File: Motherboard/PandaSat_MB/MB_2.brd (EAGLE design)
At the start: 93.9 x 89.2 mm, 165 parts, among them J1 503182-1852, J14 M023.5MM_LOCK, J15 M023.5MM_LOCK, J16 M023.5MM_LOCK, J17 10118194-0001LF, J2 10118194-0001LF, J3 USBC, J4 BU-SMA-V, J5 BK-18650, K4 PE014006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

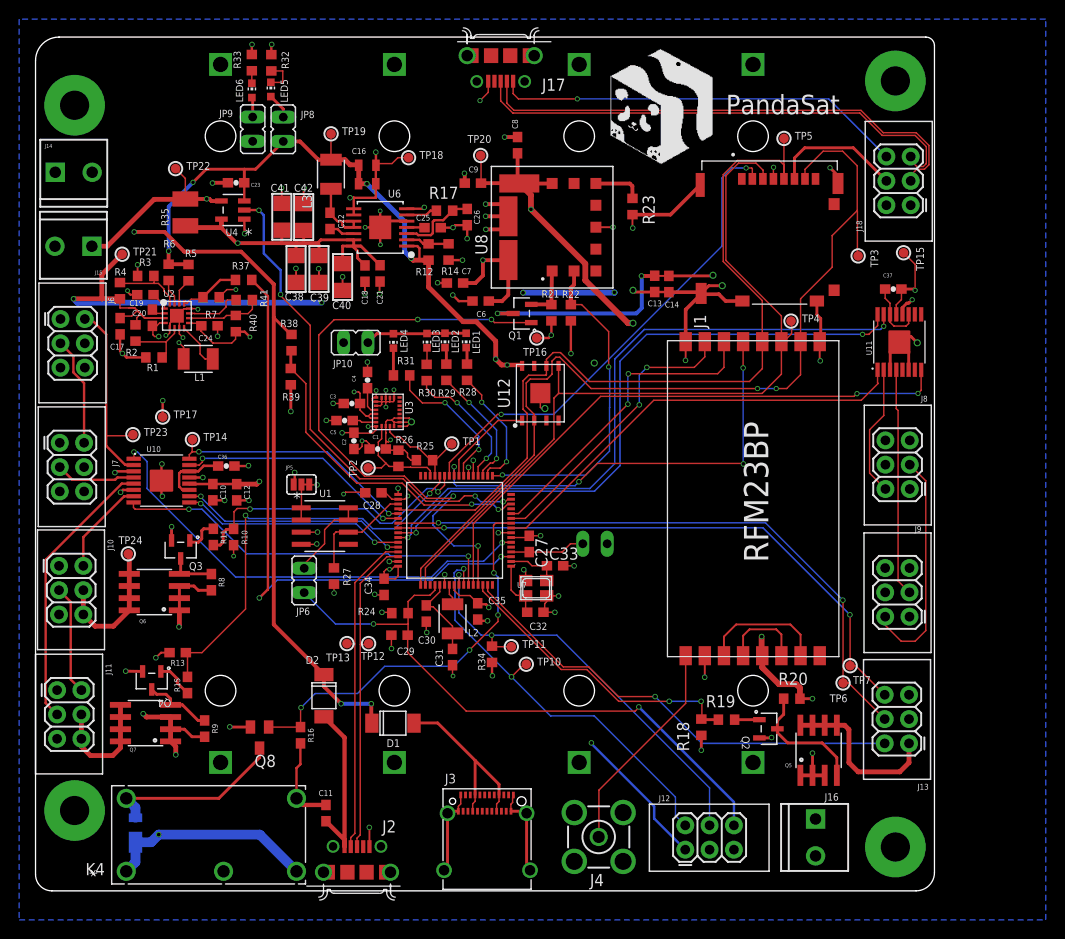
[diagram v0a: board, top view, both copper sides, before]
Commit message: Solar Panel Gerbers Final X, DRC updates for MB
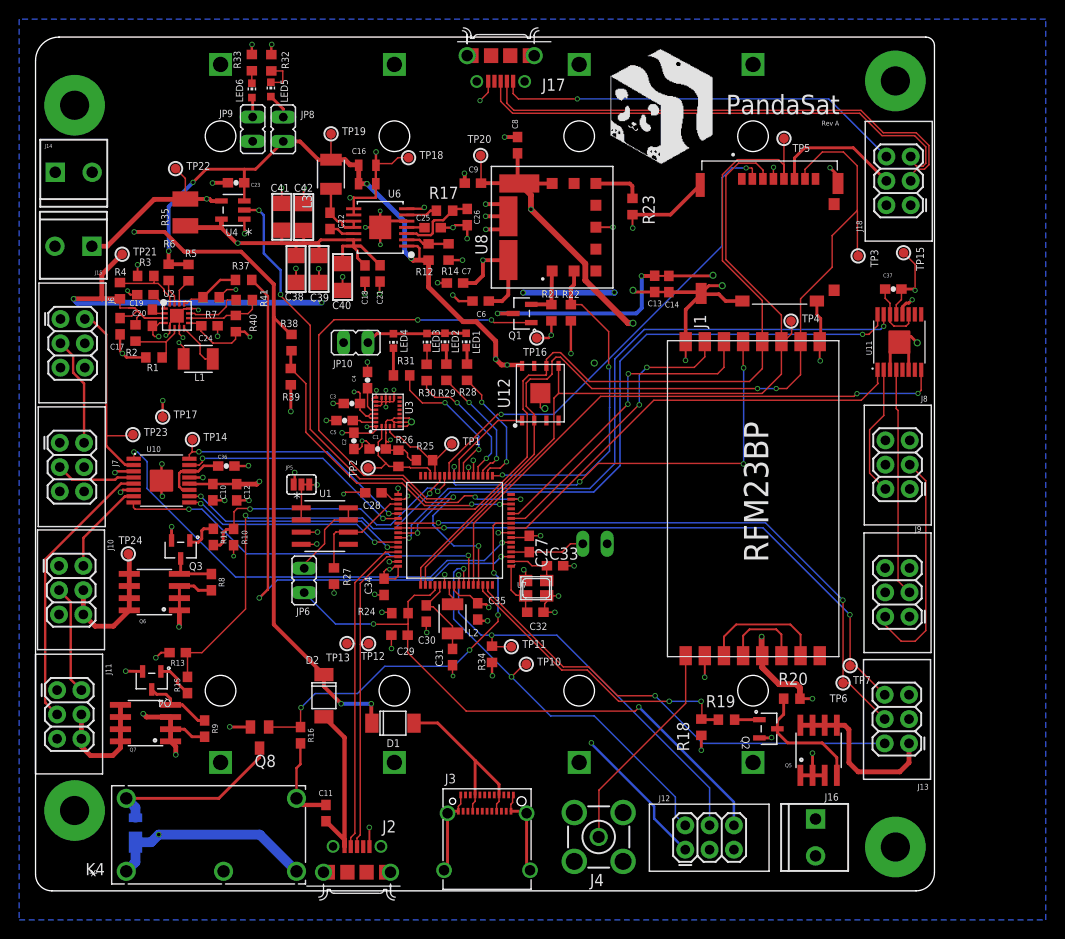
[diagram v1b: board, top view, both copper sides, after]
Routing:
- net I_BATT: track 51.3 -> 53.2 mm
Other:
- board text added: "Rev A"

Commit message: Updated DRC Rules and fixed up errors
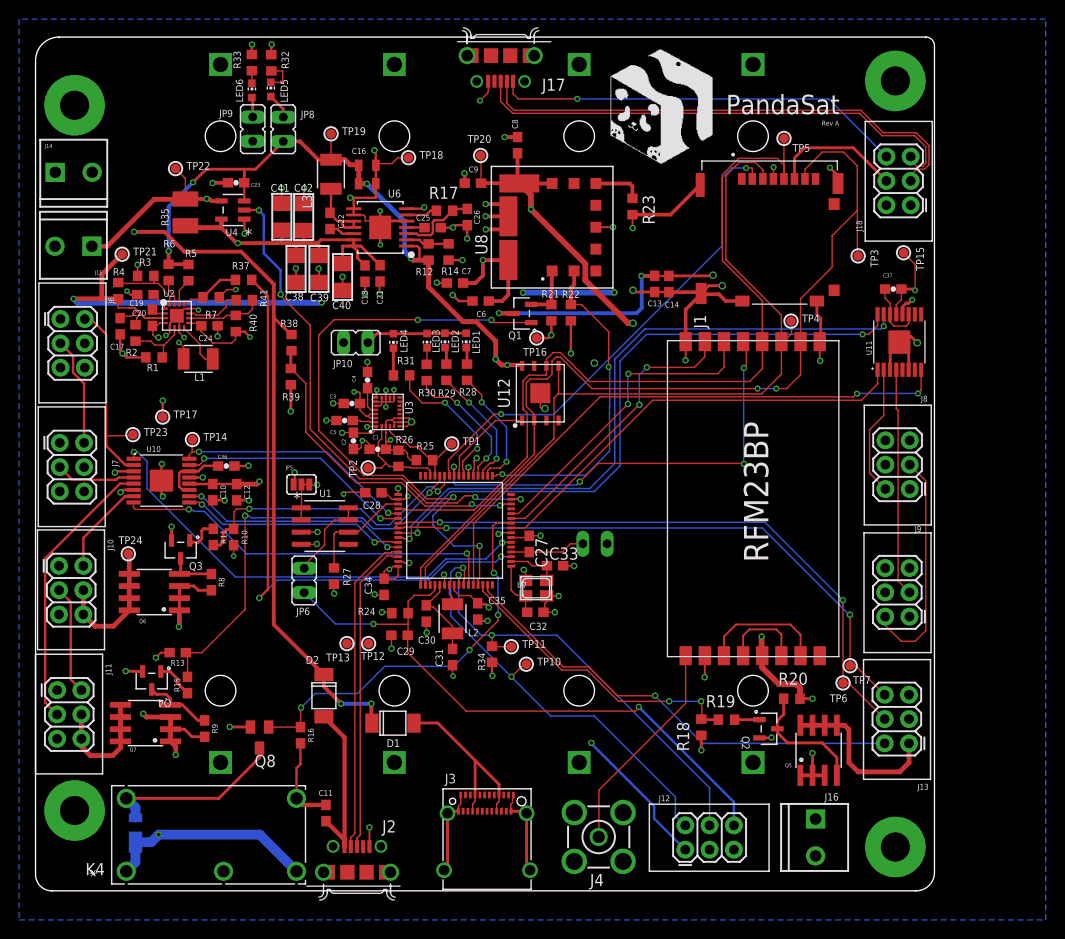
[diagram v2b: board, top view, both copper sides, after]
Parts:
- moved R4 0.18 mm to (-86.2, 63.2)
- moved C2 0.05 mm to (-61.7, 47.5)
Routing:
- net GND: track 260.4 -> 263.6 mm, vias 96 -> 95
- net SWDIO: track 44.1 -> 44.7 mm

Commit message: DRC error fixes, changed footprint for USB-C w/ milling layer
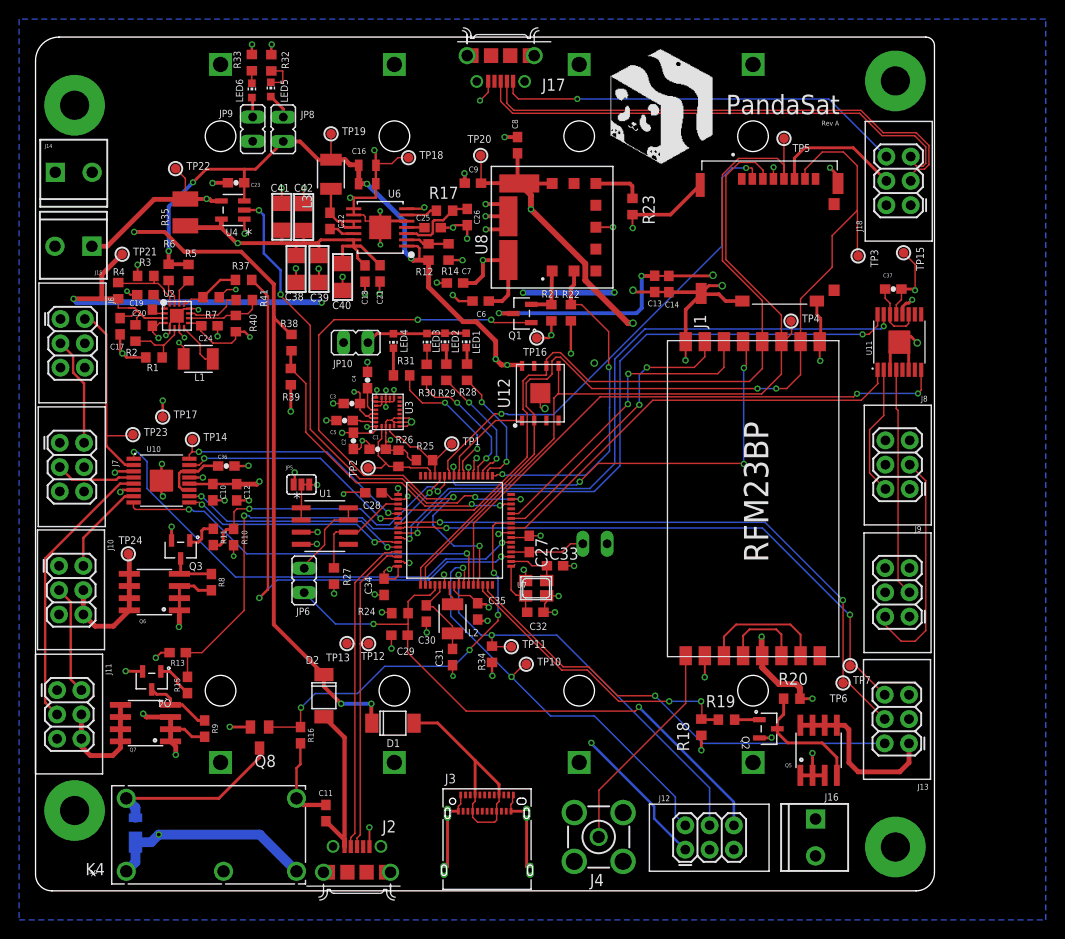
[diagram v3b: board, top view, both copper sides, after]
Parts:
- removed FRAME1, FRAME2, FRAME3, FRAME4: FRAME-LETTER, SparkFun-Aesthetics:CREATIVE_COMMONS
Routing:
- net V_CH: track 19.9 -> 24.2 mm
- net SPI_MISO: track 96.3 -> 95.7 mm

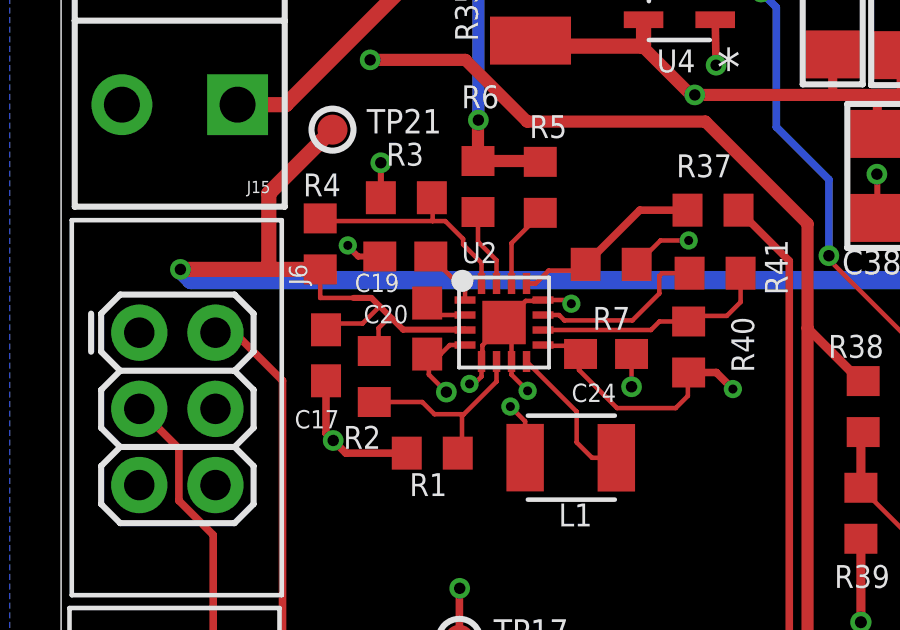
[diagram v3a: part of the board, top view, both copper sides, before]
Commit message: Changed footprint of LTC4121
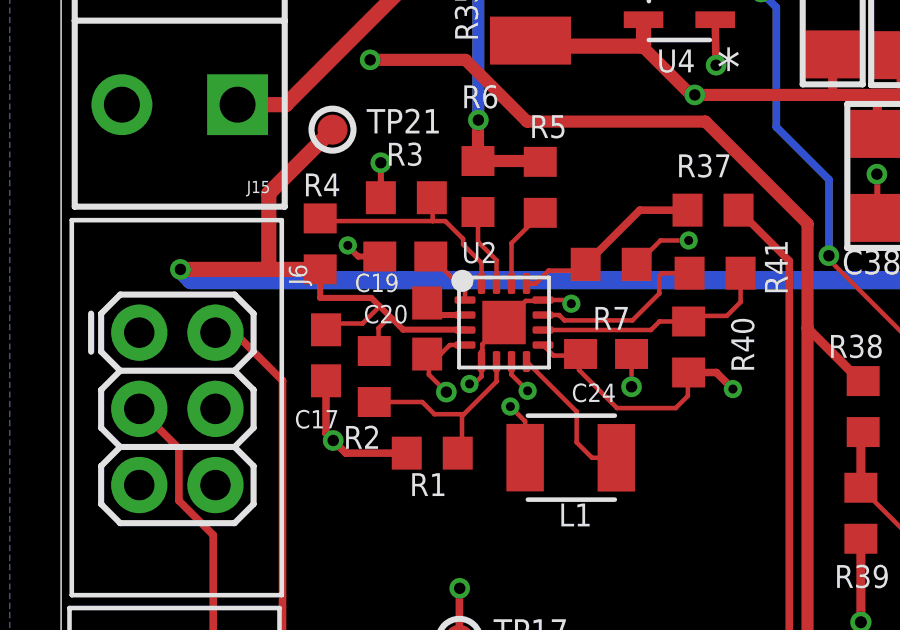
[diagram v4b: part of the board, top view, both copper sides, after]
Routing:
- net VBATT: track 234.0 -> 234.8 mm
- net GND: track 263.6 -> 263.0 mm
- net N$9: track 1.43 -> 2.02 mm

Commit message: Updated schematic + layout but have some git troubles!
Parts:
- X1: value (none) -> ECX-31B; device adafruit:NX3225 -> pandasat:ECX-31B
- moved C32 3.50 mm to (-40.2, 32.1)
- moved X1 1.75 mm to (-44.2, 31.5), turned to 90 degrees
- moved TP18 1.73 mm to (-54.2, 77.1)
- moved U5 1.40 mm to (-19.4, 43.4)
- moved TP5 1.33 mm to (-15.7, 79.9)
- moved TP4 1.19 mm to (-15.9, 61.2)
- moved J1 0.51 mm to (-18.7, 68.5)
- moved C33 0.44 mm to (-40.2, 34.3)
- moved U8 0.38 mm to (-40.9, 69.4)
- moved R15 0.36 mm to (-79.4, 22.1)
- moved C6 0.30 mm to (-48.4, 62.4)
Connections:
- net GND: no longer X1.2, X1.4
- net N$29: now also X1.1; no longer X1.3
- net N$44: now also X1.2; no longer X1.1
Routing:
- net SPI_SCK: track 88.0 -> 92.6 mm
- net GND: track 263.0 -> 267.6 mm, vias 95 -> 93
- net N$41: track 136.4 -> 138.7 mm
- net 5V: track 129.9 -> 131.8 mm
- net N$39: track 13.2 -> 11.5 mm
- net RF_SDN: track 30.6 -> 32.1 mm
- net RF_NIRQ: track 33.1 -> 34.5 mm
- net N$36: track 22.7 -> 24.1 mm
- net SPI_CS_RFM: track 47.1 -> 48.4 mm
- net P_GOOD: track 34.7 -> 33.6 mm
- net N$18: track 5.72 -> 4.56 mm
- net N$44: track 5.48 -> 4.41 mm
- net SPI_MOSI: track 84.5 -> 85.6 mm
- net 3.3V: track 193.9 -> 194.9 mm
- net N$9: track 2.02 -> 1.43 mm
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
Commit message: Fixed lib issue
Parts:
- X1: value ECX-31B -> (none)
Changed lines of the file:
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@@
 <attribute name="VALUE" x="-70.3834" y="83.4644" size="1.27" layer="27" rot="R90"/>
 </element>
-<element name="X1" library="pandasat" package="ECX-31B" value="ECX-31B" x="-44.2468" y="31.5214" smashed="yes" rot="R90">
+<element name="X1" library="pandasat" package="ECX-31B" value="" x="-44.2468" y="31.5214" smashed="yes" rot="R90">
 <attribute name="NAME" x="-42.8244" y="31.0944" size="0.5" layer="25" rot="R180"/>
 </element>

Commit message: Updates to MB
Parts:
- added B1: (no value), microbuilder:BTN_KMR2_4.6X2.8
- U7: device pandasat:TQFP64 -> pandasat:TQFP-64
- moved U7 3.61 mm to (-50.9, 38.0), turned to 0 degrees
- moved J16 3.60 mm to (-13.9, 4.26), turned to 90 degrees
- moved J14 3.56 mm to (-89.1, 75.3), turned to 180 degrees
- moved J15 3.44 mm to (-92.6, 68.1), turned to 0 degrees
- moved C28 0.74 mm to (-60.0, 41.4)
- moved C27 0.16 mm to (-43.2, 36.7)
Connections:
- net !RESET: now also B1.B, B1.B'
- net GND: now also B1.A, B1.A'
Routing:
- net GND: track 267.6 -> 276.9 mm, vias 93 -> 95
- net VBATT: track 234.8 -> 243.4 mm
- net VBATT_IN: track 115.6 -> 124.2 mm
- net !RESET: track 65.2 -> 70.3 mm
- net N$59: track 28.1 -> 31.9 mm
- net MINY_2: track 68.3 -> 69.6 mm
- net I_BATT: track 53.2 -> 54.0 mm
- net 5V_EN: track 63.8 -> 64.6 mm
- net SWCLK: track 46.4 -> 47.1 mm
- net SWDIO: track 44.7 -> 45.3 mm
- net SPI_CS_RFM: track 48.4 -> 49.1 mm
- net SPI_SCK: track 92.6 -> 92.0 mm
- net N$4: track 7.80 -> 7.22 mm
- net DXZ_FAULT: track 40.8 -> 41.3 mm
- net DY_FAULT: track 61.1 -> 61.6 mm
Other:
- outline, holes or cut-outs redrawn

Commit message: Readded frames on schematics
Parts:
- added FRAME1, FRAME2, FRAME3, FRAME4: FRAME-LETTER, SparkFun-Aesthetics:CREATIVE_COMMONS
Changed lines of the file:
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@@
 <?xml version="1.0" encoding="utf-8"?>
 <!DOCTYPE eagle SYSTEM "eagle.dtd">
-<eagle version="9.2.2">
+<eagle version="9.3.0">
 <drawing>
 <settings>
@@
 <attribute name="VALUE" x="-42.6466" y="19.558" size="0.4064" layer="27" ratio="10" rot="R180"/>
 </element>
+<element name="FRAME1" library="SparkFun-Aesthetics" library_urn="urn:adsk.eagle:library:507" package="CREATIVE_COMMONS" package3d_urn="urn:adsk.eagle:package:37121/1" value="FRAME-LETTER" x="-76.28" y="-14.99" smashed="yes"/>
+<element name="FRAME2" library="SparkFun-Aesthetics" library_urn="urn:adsk.eagle:library:507" package="CREATIVE_COMMONS" package3d_urn="urn:adsk.eagle:package:37121/1" value="FRAME-LETTER" x="-76.28" y="-23.65" smashed="yes"/>
+<element name="FRAME3" library="SparkFun-Aesthetics" library_urn="urn:adsk.eagle:library:507" package="CREATIVE_COMMONS" package3d_urn="urn:adsk.eagle:package:37121/1" value="FRAME-LETTER" x="-76.28" y="-32.31" smashed="yes"/>
+<element name="FRAME4" library="SparkFun-Aesthetics" library_urn="urn:adsk.eagle:library:507" package="CREATIVE_COMMONS" package3d_urn="urn:adsk.eagle:package:37121/1" value="FRAME-LETTER" x="-76.28" y="-40.97" smashed="yes"/>
 </elements>
 <signals>
